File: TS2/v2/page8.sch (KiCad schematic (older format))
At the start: 10 parts, among them U28 74LS148, U32 74LS138, U33 74LS138

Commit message: Add some notes about interrupt circuitry.
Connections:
- net IACK7*: now reaches U33.7 (O7)
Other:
- note removed: "IACK7*"
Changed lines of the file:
@@
 Rev "2.0"
 Comp "Jeff Tranter"
-Comment1 "Interrupt Control Circuitry"
+Comment1 "Interrupt Control Circuitry (optional)"
 Comment2 ""
 Comment3 ""
@@
 Text Label 8550 4650 2    60   ~ 0
 IACK6*
-Text Notes 8550 4750 2    60   ~ 0
-IACK7*
 NoConn ~ 8550 4750
 NoConn ~ 8550 4650
@@
 NoConn ~ 8550 4250
 NoConn ~ 8550 4150
+Text Label 8550 4750 2    60   ~ 0
+IACK7*
 $EndSCHEMATC

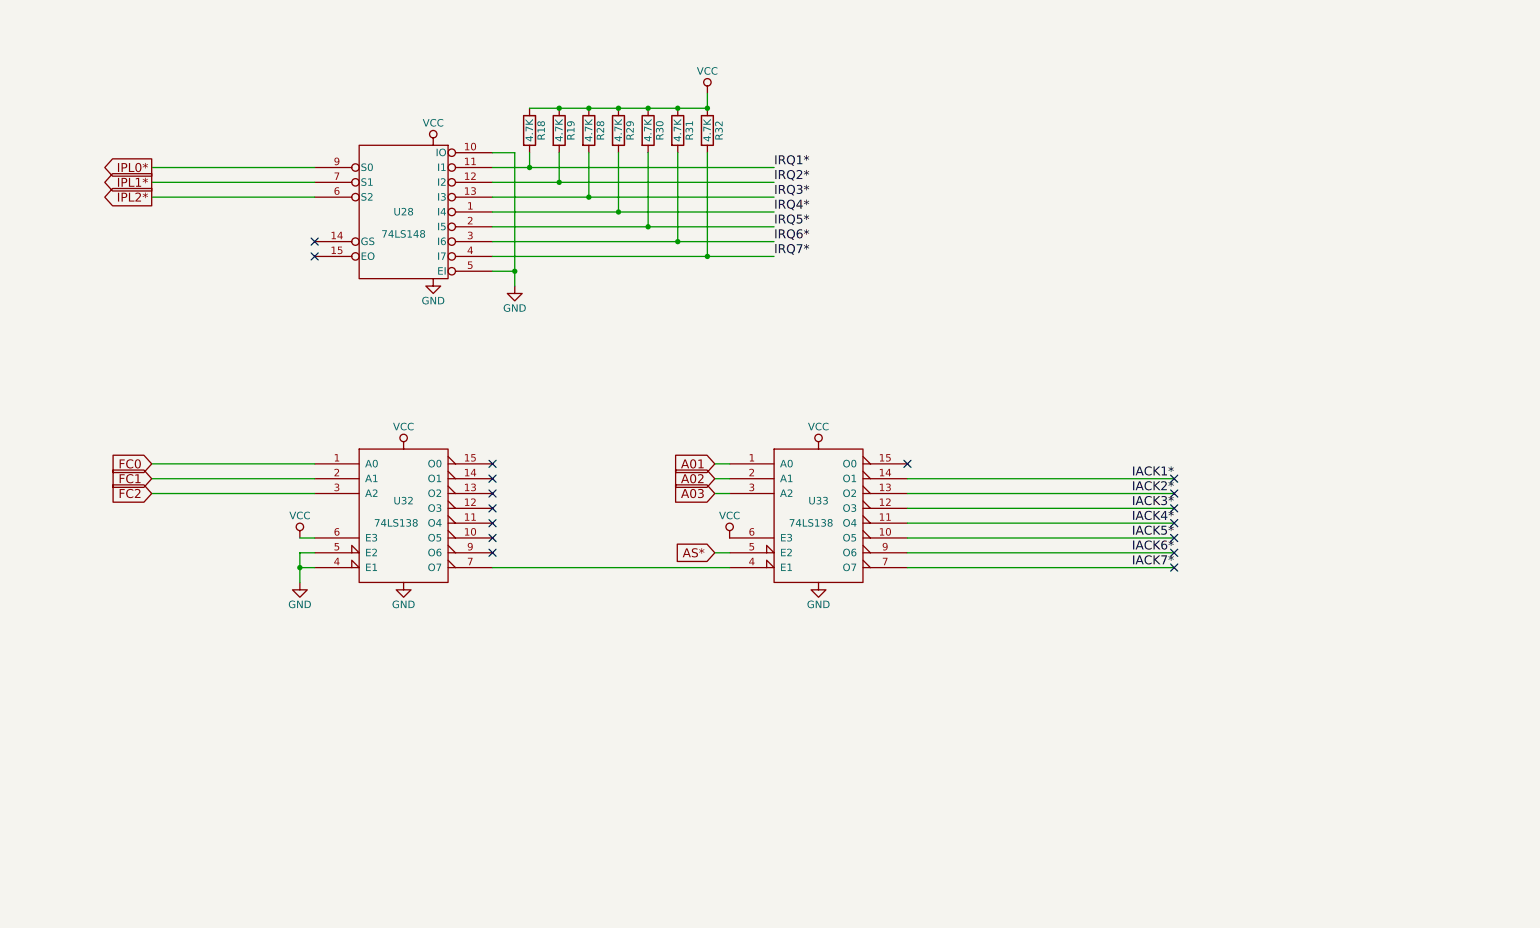
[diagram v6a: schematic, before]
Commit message: Implementing more of interrupt circuitry.
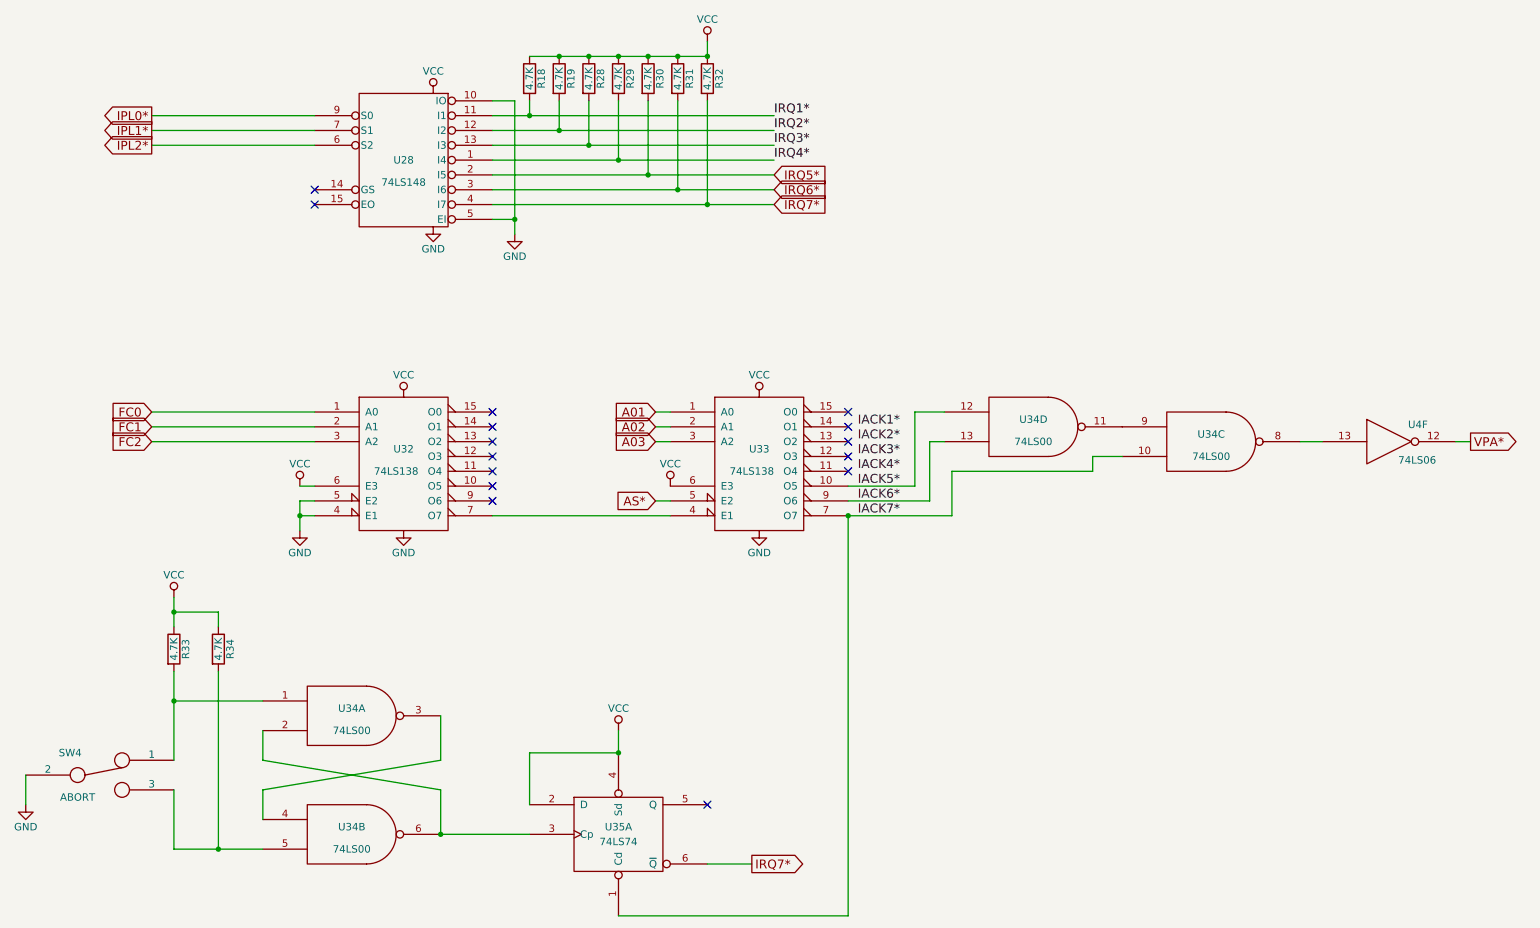
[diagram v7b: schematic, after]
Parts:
- added R33, R34: 4.7K, symbol R
- added SW4: ABORT, symbol SWITCH_INV
- added U34: 74LS00, symbol 74LS00
- added U35: 74LS74, symbol 74LS74
- added U4: 74LS06, symbol 74LS06
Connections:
- net GND: now also SW4.2, U34.7 (GND), U34.7 (GND), U34.7 (GND), U34.7 (GND), U35.7 (GND), U4.7 (GND)
- net IACK1*: no longer U33.14 (O1)
- net IACK2*: no longer U33.13 (O2)
- net IACK3*: no longer U33.12 (O3)
- net IACK4*: no longer U33.11 (O4)
- net IACK5*: now also U34.12
- net IACK6*: now also U34.13
- net IACK7*: now also U34.10, U35.1 (Cd)
- net IRQ7*: now also U35.6 (~Q)
- net VCC: now also R33.1, R34.1, U34.14 (VCC), U34.14 (VCC), U34.14 (VCC), U34.14 (VCC), U35.14 (VCC), U35.2 (D), U35.4 (Sd), U4.14 (VCC)
- new net: R33.2, SW4.1, U34.1
- new net: U34.2, U34.6, U35.3 (Cp)
- new net: U34.3, U34.4
- new net: R34.2, SW4.3, U34.5
- new net: U34.8, U4.13
- new net: U34.11, U34.9
- new net VPA*: U4.12
- no-connect marks 17 -> 15
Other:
- moved on the sheet: R18, R19, R28, R29, R30, R31, R32, U28, U32, U33

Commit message: Add some notes and signal names.
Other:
- note added: "7 levels of interrupt acknowledge"
- note added: "7 levels of\ninterrupt\nrequest"
- note added: "Function\ncodes\n0-7"
- note added: "IACK*"
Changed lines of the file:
@@
 Wire Wire Line
 	3950 4400 5150 4400
+Text Notes 6350 2050 0    60   ~ 0
+7 levels of\ninterrupt\nrequest
+Text Notes 6200 3500 0    60   ~ 0
+7 levels of interrupt acknowledge
+Text Notes 4250 4550 0    60   ~ 0
+IACK*
+Text Notes 4100 4100 0    60   ~ 0
+Function\ncodes\n0-7
 $EndSCHEMATC
